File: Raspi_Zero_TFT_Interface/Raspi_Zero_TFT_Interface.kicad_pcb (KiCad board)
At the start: 4 copper layers, 39 parts, among them CN1 USB_C_Receptacle_PowerOnly_6P, CN2 B2B-XH-A, CN3 Molex FPC 541044031, CN4 Molex FPC 52271-0679, CN5 Conn_02x20_Odd_Even, J1 522070860, Q1 SI2347DS-TI-GE3CT, Q3 DMG3406L-7, Q4 SSM3J358R, SW2 Rocker Switch SPST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

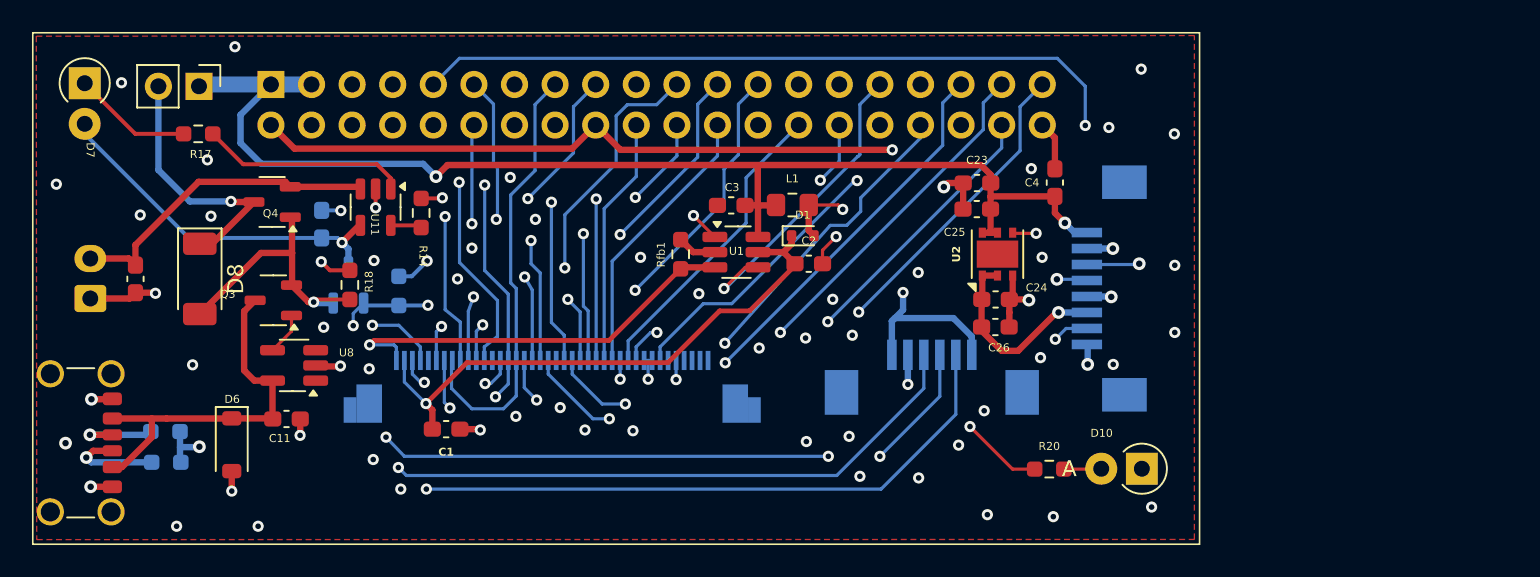
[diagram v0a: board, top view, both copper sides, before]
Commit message: Finished Rasp Board PCB Routing
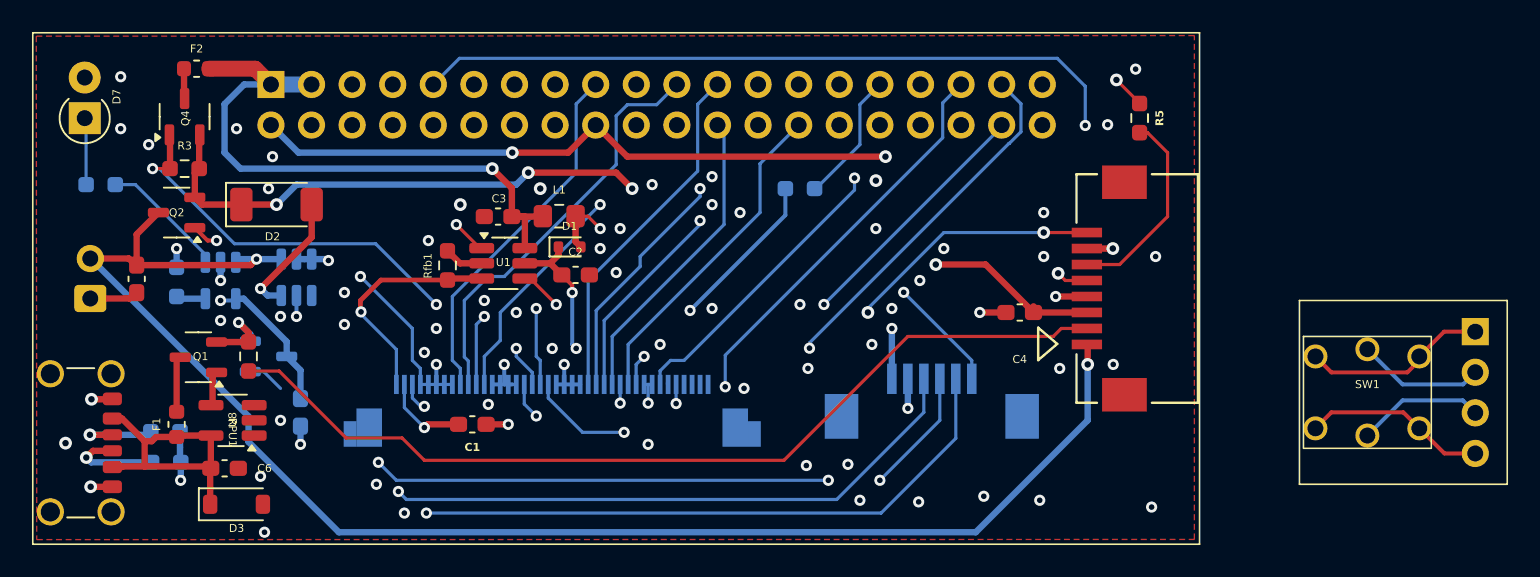
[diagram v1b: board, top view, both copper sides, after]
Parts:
- removed C11: 0.1u, Capacitor_SMD:C_0603_1608Metric_Pad1.08x0.95mm_HandSolder
- removed C23, C24: 1uF/XR5, Capacitor_SMD:C_0603_1608Metric_Pad1.08x0.95mm_HandSolder
- removed C25, C26: 100n, Capacitor_SMD:C_0603_1608Metric_Pad1.08x0.95mm_HandSolder
- removed D10: LED, Diode_THT:D_T-1_P2.54mm_Vertical_AnodeUp
- removed D6: NC, Diode_SMD:D_SOD-123
- removed D8: PMEG3030EP,115, Diode_SMD:D_SOD-128
- removed R18: 10k, Resistor_SMD:R_0603_1608Metric_Pad0.98x0.95mm_HandSolder
- removed R20: 1k, Resistor_SMD:R_0603_1608Metric_Pad0.98x0.95mm_HandSolder
- removed SW2: Rocker Switch SPST, Connector_PinHeader_2.54mm:PinHeader_1x02_P2.54mm_Vertical
- removed U2: LD39200, Package_DFN_QFN:DFN-6-1EP_3x3mm_P0.95mm_EP1.7x2.6mm
- added C6: 0.1u, Capacitor_SMD:C_0603_1608Metric_Pad1.08x0.95mm_HandSolder, F.Cu at (5.50, 26.2)
- added D2: PMEG3030EP,115, Diode_SMD:D_SOD-128, F.Cu at (8.75, 9.75)
- added D3: NC, Diode_SMD:D_SOD-123, F.Cu at (6.25, 28.5)
- added F1: 1.5 A Slow-Blow, Fuse:Fuse_0603_1608Metric, F.Cu at (2.50, 23.5)
- added F2: 1.5 A Slow-Blow, Fuse:Fuse_0603_1608Metric, F.Cu at (3.75, 1.25)
- added J2: Conn_01x04_Pin, Connector_PinHeader_2.54mm:PinHeader_1x04_P2.54mm_Vertical, B.Cu at (83.8, 17.7)
- added Q2: SSM3J358R, Package_TO_SOT_SMD:SOT-23-3, F.Cu at (2.50, 10.2)
- added R3: 10k, Resistor_SMD:R_0603_1608Metric_Pad0.98x0.95mm_HandSolder, F.Cu at (3.00, 7.50)
- added R4: 33, Resistor_SMD:R_0603_1608Metric_Pad0.98x0.95mm_HandSolder, B.Cu at (41.5, 8.75)
- added R5: 33, Resistor_SMD:R_0603_1608Metric_Pad0.98x0.95mm_HandSolder, F.Cu at (62.8, 4.34)
- added SW1: Off-mom push button, GenII:TL1240_LED_Switch, F.Cu at (77.0, 21.5)
- added U3: LTC4412xS6, Package_TO_SOT_SMD:TSOT-23-6, B.Cu at (10.0, 14.3)
- J1: moved to F.Cu
- Q1: value SI2347DS-TI-GE3CT -> DMG3406L-7; moved to F.Cu
- Q3: value DMG3406L-7 -> SSM3J358R; moved to B.Cu
- R14, R17, U11: moved to B.Cu
- RPU1: value 5k -> 10k; moved to F.Cu
- Rfb1: value 6.25 -> 13
- moved R14 15.9 mm to (2.50, 14.6)
- moved C2 14.6 mm to (27.5, 14.2)
- moved Rfb1 14.6 mm to (19.4, 13.6)
- moved C3 14.6 mm to (22.6, 10.5)
- moved D1 14.6 mm to (27.1, 12.4)
- moved L1 14.6 mm to (26.4, 10.5)
- moved U1 14.6 mm to (22.9, 13.4)
- moved C19 11.8 mm to (10.2, 22.8), turned to 90 degrees
- moved U11 10.7 mm to (5.25, 14.5)
- moved Q1 10.4 mm to (3.86, 19.3), turned to 180 degrees
- moved RPU1 10.3 mm to (7.00, 19.2), turned to -90 degrees
- moved C4 8.42 mm to (55.2, 16.5), turned to 180 degrees
- moved Q4 7.65 mm to (3.00, 4.25), turned to 90 degrees
- moved R17 6.88 mm to (-2.25, 8.50)
- moved U8 5.16 mm to (6.00, 23.2)
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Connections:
- C3 pad 1: /Vcc -> /Vcc_Pi_Screen
- C4 pad 1: /Vcc -> /Vcc_MeasBoard
- CN3 pad 17: /B3 -> /3V3_Pi
- CN3 pad 18: /B2 -> /3V3_Pi
- CN3 pad 19: /B1 -> /3V3_Pi
- CN3 pad 20: /B0 -> /3V3_Pi
- CN3 pad 25: /G3 -> /3V3_Pi
- CN3 pad 26: /G2 -> /3V3_Pi
- CN3 pad 27: /G1 -> /3V3_Pi
- CN3 pad 28: /G0 -> /3V3_Pi
- CN3 pad 33: /G3 -> /3V3_Pi
- CN3 pad 34: /G2 -> /3V3_Pi
- CN3 pad 35: /R1 -> /3V3_Pi
- CN3 pad 36: /R0 -> /3V3_Pi
- CN4 pad 1: /3V3_Pi -> /~{RESET}
- CN5 pad 1: /Vcc -> /Vcc_Pi_Screen
- CN5 pad 15: /G3 -> unconnected-(CN5-Pin_15-Pad15)
- CN5 pad 16: /G2 -> /~{RESET}
- CN5 pad 25: /B3 -> unconnected-(CN5-Pin_25-Pad25)
- CN5 pad 3: /Vcc -> /Vcc_Pi_Screen
- CN5 pad 30: /B1 -> unconnected-(CN5-Pin_30-Pad30)
- CN5 pad 31: /PWM_EN -> Net-(CN5-Pin_31)
- CN5 pad 32: /B2 -> unconnected-(CN5-Pin_32-Pad32)
- CN5 pad 34: /G1 -> unconnected-(CN5-Pin_34-Pad34)
- CN5 pad 39: /R1 -> unconnected-(CN5-Pin_39-Pad39)
- CN5 pad 7: /UART_TX -> Net-(CN5-Pin_7)
- J1 pad 1: /Vcc -> /V_Batt
- J1 pad 2: GND -> /~{CHARGE_EN}
- J1 pad 3: /UART_TX -> /Vcc_MeasBoard
- J1 pad 4: /UART_RX -> GND
- J1 pad 5: GND -> /UART_RX
- J1 pad 6: /3V3_Main -> /UART_TX
- J1 pad 7: /~{CHARGE_EN} -> GND
- J1 pad 8: /V_Batt -> /~{PWR_EN}
- L1 pad 1: /Vcc -> /Vcc_Pi_Screen
- Q1 pad 1: /~{CHARGE_EN} -> Net-(Q1-G)
- Q1 pad 2: /Power_Management_Minimal/5V_USB -> /Power_Management_Minimal/InputVoltageProtection/Vout
- Q1 pad 3: Net-(D7-A) -> Net-(Q1-D)
- Q3 pad 1: Net-(Q3-G) -> /~{CHARGE_EN}
- Q3 pad 2: /Power_Management_Minimal/5V_USB -> /Power_Management_Minimal/InputVoltageProtection/Vout
- Q3 pad 3: /Power_Management_Minimal/VBus -> Net-(D7-A)
- Q4 pad 1: /Power_Management_Minimal/5V_USB -> /~{PWR_EN}
- Q4 pad 2: /V_Batt -> /Vcc_MeasBoard
- RPU1 pad 1: /~{CHARGE_EN} -> /Power_Management_Minimal/InputVoltageProtection/Vout
- RPU1 pad 2: GND -> /~{CHARGE_EN}
- U1 pad 6: /Vcc -> /Vcc_Pi_Screen
- U8 pad 4: Net-(Q3-G) -> Net-(Q1-G)
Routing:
- net /Vcc: track 78.4 -> 0.00 mm, vias 2 -> 0
- net /~{PWR_EN}: track 0.00 -> 69.5 mm, vias 0 -> 4
- net /Vcc_MeasBoard: track 0.00 -> 64.6 mm, vias 0 -> 4
- net /UART_TX: track 62.5 -> 12.6 mm, vias 1 -> 0
- net Net-(CN5-Pin_7): track 0.00 -> 48.9 mm, vias 0 -> 1
- net /R1: track 47.7 -> 0.00 mm, vias 2 -> 0
- net /Vcc_Pi_Screen: track 0.00 -> 38.7 mm, vias 0 -> 1
- net /G1: track 37.2 -> 0.00 mm, vias 2 -> 0
- net /B2: track 35.7 -> 0.00 mm, vias 1 -> 0
- net /~{RESET}: track 0.00 -> 33.8 mm, vias 0 -> 1
- net /B1: track 31.6 -> 0.00 mm, vias 2 -> 0
- net /G3: track 27.5 -> 0.00 mm
- net /G2: track 26.5 -> 0.00 mm, vias 3 -> 0
- net /B3: track 24.7 -> 0.00 mm, vias 2 -> 0
- net Net-(U2-PWRGD): track 20.4 -> 0.00 mm, vias 2 -> 0
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
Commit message: Final Rev3 Commit Post Submission
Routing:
- net /LED-: track 14.3 -> 16.6 mm
- net /~{PWR_EN}: track 69.5 -> 71.7 mm
- net /3V3_Pi: track 98.0 -> 99.7 mm
- net /G6: track 23.9 -> 25.2 mm
- net /R5: track 26.0 -> 25.4 mm
- net /PWM_EN: track 22.0 -> 21.5 mm
- net /~{CHARGE_EN}: track 60.5 -> 60.4 mm, vias 0 -> 2
- net GND: vias 74 -> 72
